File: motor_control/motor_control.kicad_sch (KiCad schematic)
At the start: 25 parts, among them J1 GPIO, J2 MotA, J3 MotB, J4 MOT_POW, J5 UART, J6 SPI, J7 I2C, J8 PEB_5V_IN, SW1 PU, SW2 PD, SW3 SW_SPDT_312, U1 HC-SR04

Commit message: update schematic text labels
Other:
- note added: "From PEB"
- note added: "To RPi"
- moved on the sheet: JP1
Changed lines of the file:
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@@
 		)
 	)
+	(text "From PEB"
+		(exclude_from_sim no)
+		(at 104.902 17.272 0)
+		(effects
+			(font
+				(size 1.27 1.27)
+			)
+		)
+	)
 	(text "From power expansion board"
 		(exclude_from_sim no)
@@
 		)
 	)
+	(text "To RPi"
+		(exclude_from_sim no)
+		(at 126.746 20.32 0)
+		(effects
+			(font
+				(size 1.27 1.27)
+			)
+		)
+	)
 	(text "To Motors"
 		(exclude_from_sim no)
@@
 	(wire
 		(pts
-			(xy 102.87 21.59) (xy 102.87 27.94)
+			(xy 95.25 21.59) (xy 95.25 27.94)
 		)
 		(stroke
@@
 	(wire
 		(pts
-			(xy 127 27.94) (xy 127 24.13)
+			(xy 119.38 27.94) (xy 119.38 24.13)
 		)
 		(stroke
@@
 	(wire
 		(pts
-			(xy 102.87 27.94) (xy 109.22 27.94)
+			(xy 95.25 27.94) (xy 101.6 27.94)
 		)
 		(stroke
@@
 	(wire
 		(pts
-			(xy 119.38 27.94) (xy 127 27.94)
+			(xy 111.76 27.94) (xy 119.38 27.94)
 		)
 		(stroke
@@
 	(symbol
 		(lib_id "power:+5V")
-		(at 102.87 21.59 0)
+		(at 95.25 21.59 0)
 		(unit 1)
 		(exclude_from_sim no)
@@
 		(dnp no)
 		(property "Reference" "#PWR031"
-			(at 102.87 25.4 0)
+			(at 95.25 25.4 0)
 			(effects
 				(font
@@
 		)
 		(property "Value" "5V_IN"
-			(at 103.2383 17.2656 0)
+			(at 95.6183 17.2656 0)
 			(effects
 				(font
@@
 		)
 		(property "Footprint" ""
-			(at 102.87 21.59 0)
+			(at 95.25 21.59 0)
 			(effects
 				(font
@@
 		)
 		(property "Datasheet" ""
-			(at 102.87 21.59 0)
+			(at 95.25 21.59 0)
 			(effects
 				(font
@@
 		)
 		(property "Description" "Power symbol creates a global label with name \"+5V\""
-			(at 102.87 21.59 0)
+			(at 95.25 21.59 0)
 			(effects
 				(font
@@
 	(symbol
 		(lib_id "power:+5V")
-		(at 127 24.13 0)
+		(at 119.38 24.13 0)
 		(unit 1)
 		(exclude_from_sim no)
@@
 		(dnp no)
 		(property "Reference" "#PWR030"
-			(at 127 27.94 0)
+			(at 119.38 27.94 0)
 			(effects
 				(font
@@
 		)
 		(property "Value" "+5V"
-			(at 127.3683 19.8056 0)
+			(at 119.7483 19.8056 0)
 			(effects
 				(font
@@
 		)
 		(property "Footprint" ""
-			(at 127 24.13 0)
+			(at 119.38 24.13 0)
 			(effects
 				(font
@@
 		)
 		(property "Datasheet" ""
-			(at 127 24.13 0)
+			(at 119.38 24.13 0)
 			(effects
 				(font
@@
 		)
 		(property "Description" "Power symbol creates a global label with name \"+5V\""
-			(at 127 24.13 0)
+			(at 119.38 24.13 0)
 			(effects
 				(font
@@
 	(symbol
 		(lib_id "Jumper:Jumper_2_Open")
-		(at 114.3 27.94 0)
+		(at 106.68 27.94 0)
 		(unit 1)
 		(exclude_from_sim no)
@@
 		(fields_autoplaced yes)
 		(property "Reference" "JP1"
-			(at 114.3 21.59 0)
+			(at 106.68 21.59 0)
 			(effects
 				(font
@@
 		)
 		(property "Value" "5V_PEB_RPi"
-			(at 114.3 24.13 0)
+			(at 106.68 24.13 0)
 			(effects
 				(font
@@
 		)
 		(property "Footprint" "Connector_PinHeader_2.54mm:PinHeader_1x02_P2.54mm_Vertical"
-			(at 114.3 27.94 0)
+			(at 106.68 27.94 0)
 			(effects
 				(font
@@
 		)
 		(property "Datasheet" "~"
-			(at 114.3 27.94 0)
+			(at 106.68 27.94 0)
 			(effects
 				(font
@@
 		)
 		(property "Description" "Jumper, 2-pole, open"
-			(at 114.3 27.94 0)
+			(at 106.68 27.94 0)
 			(effects
 				(font

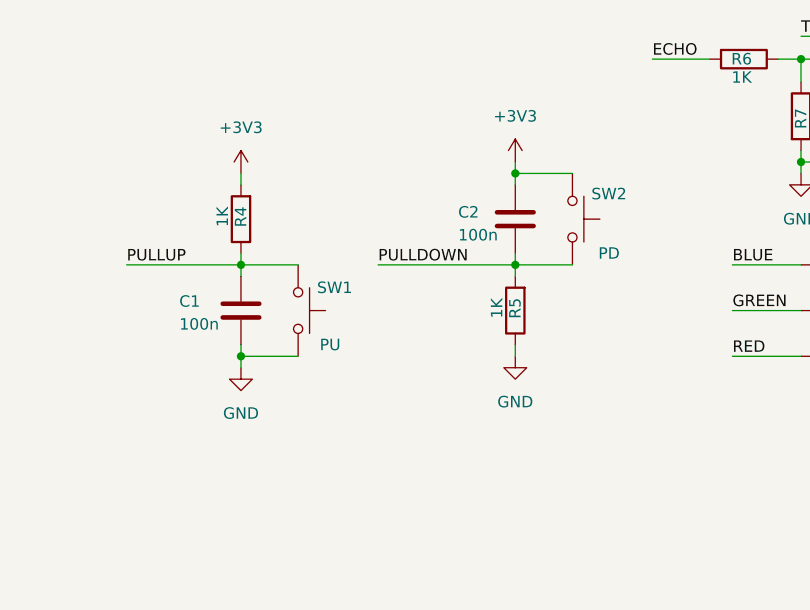
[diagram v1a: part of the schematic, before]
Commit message: update pull-down debouncer
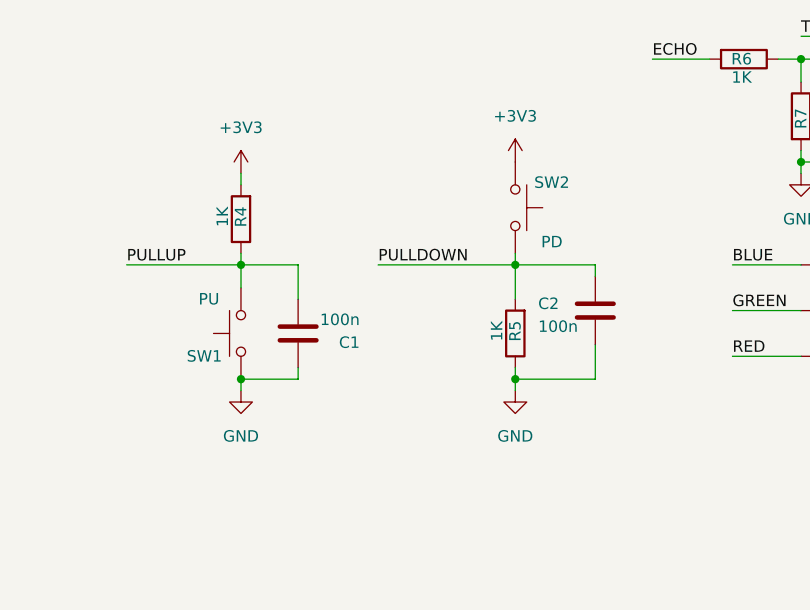
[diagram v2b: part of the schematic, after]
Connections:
- net +3V3: no longer C2.2
- net GND: now also C1.2, C2.1, SW1.1; no longer C1.1, SW1.2
- net PULLDOWN: now also C2.2; no longer C2.1
- net PULLUP: now also C1.1, SW1.2; no longer C1.2, SW1.1
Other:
- moved on the sheet: C1, C2, R5, SW1, SW2

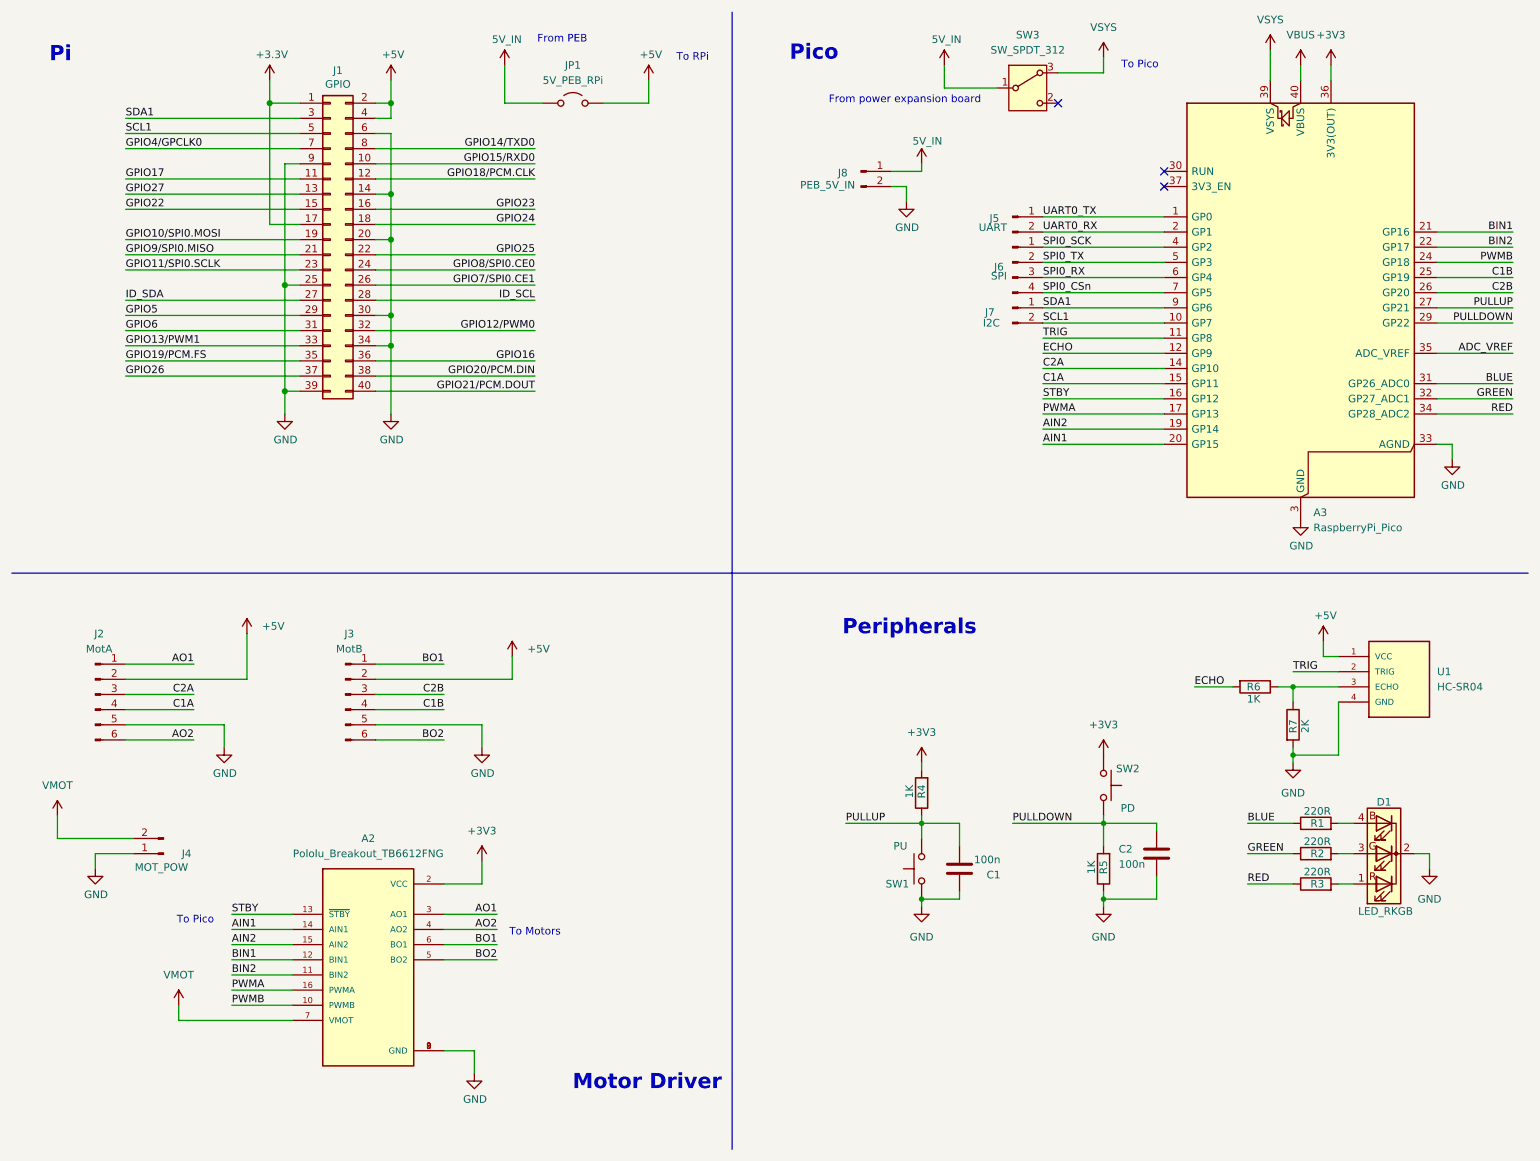
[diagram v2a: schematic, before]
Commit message: update REG_5V as source for all 5V components
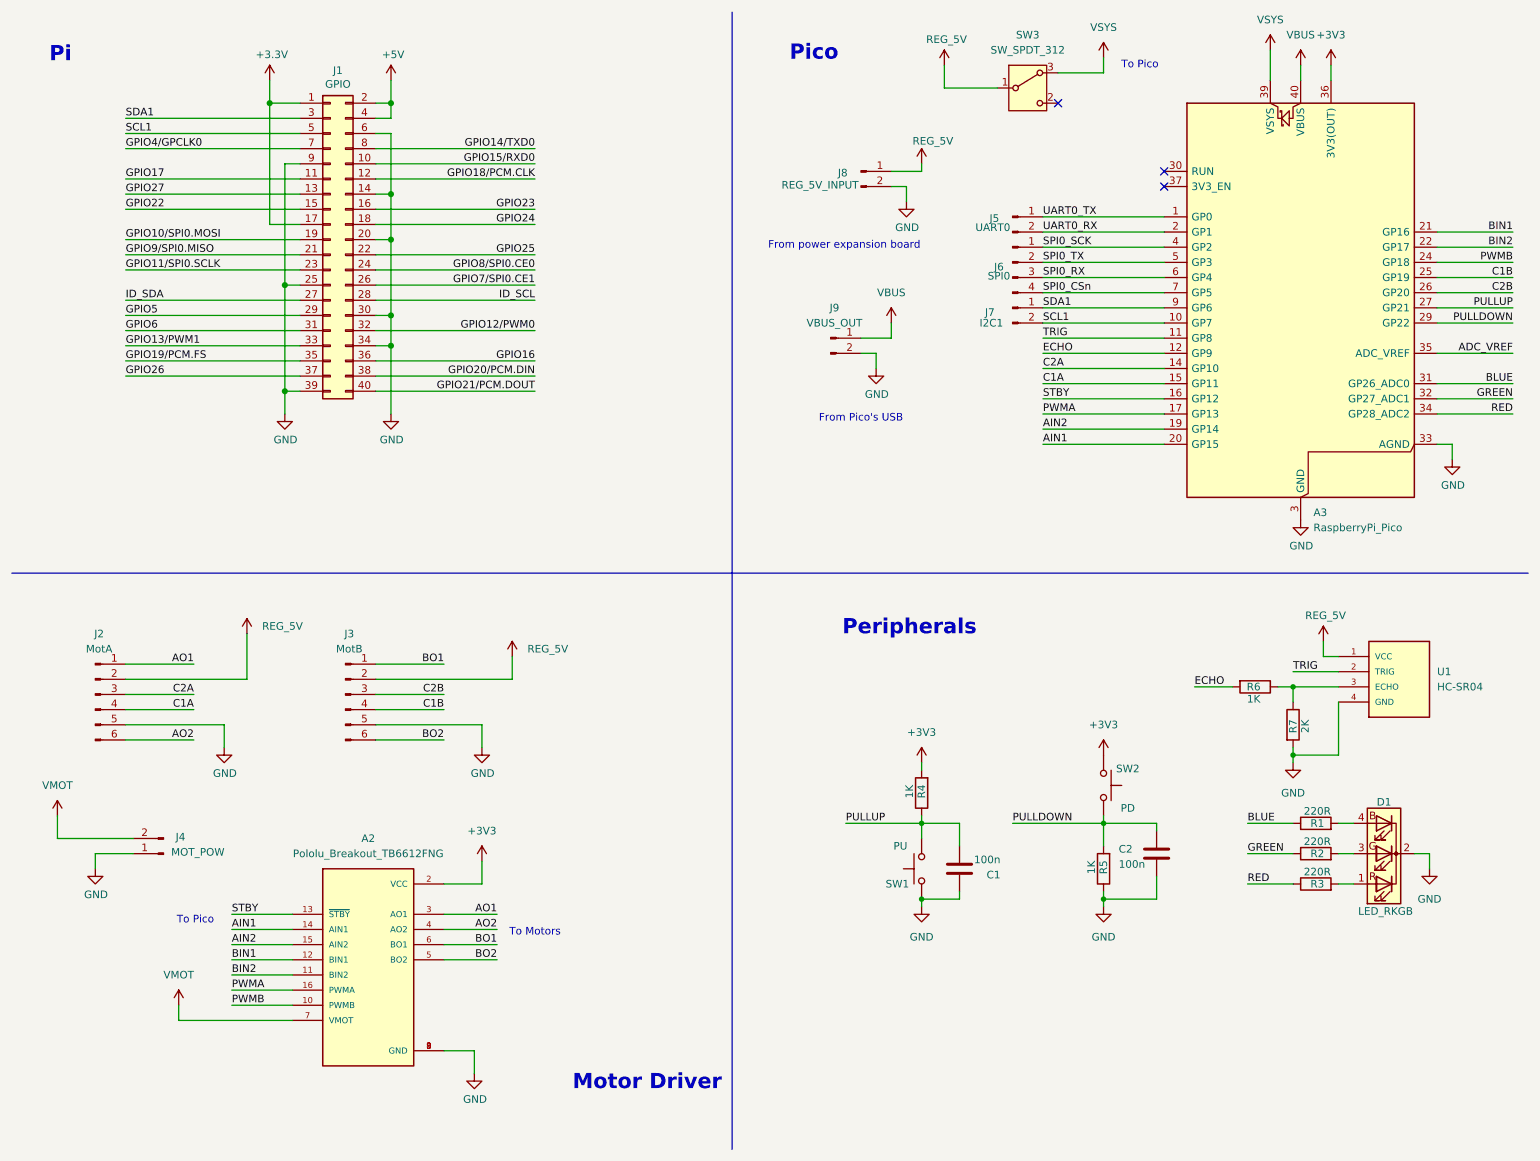
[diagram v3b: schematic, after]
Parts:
- removed JP1: 5V_PEB_RPi, Connector_PinHeader_2.54mm:PinHeader_1x02_P2.54mm_Vertical, symbol Jumper:Jumper_2_Open
- added J9: VBUS_OUT, symbol Connector:Conn_01x02_Pin
- J5: value UART -> UART0
- J6: value SPI -> SPI0
- J7: value I2C -> I2C1
- J8: value PEB_5V_IN -> REG_5V_INPUT
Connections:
- net +5V: no longer J2.2 (Pin_2), J3.2 (Pin_2), U1.1 (VCC)
- net GND: now also J9.2 (Pin_2)
- net VBUS: now also J9.1 (Pin_1)
- net 5V_IN renamed REG_5V
- net REG_5V: now also J2.2 (Pin_2), J3.2 (Pin_2), U1.1 (VCC)
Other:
- note added: "From Pico's USB"
- note removed: "From PEB"
- note removed: "To RPi"

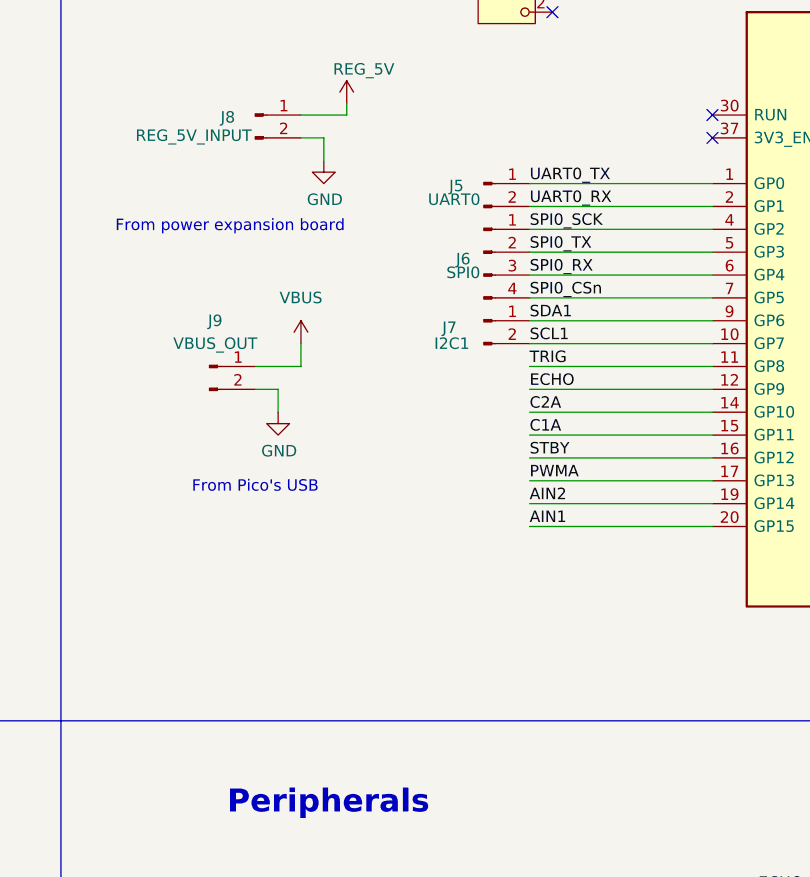
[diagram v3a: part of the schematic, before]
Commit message: update unused GP pins net labels
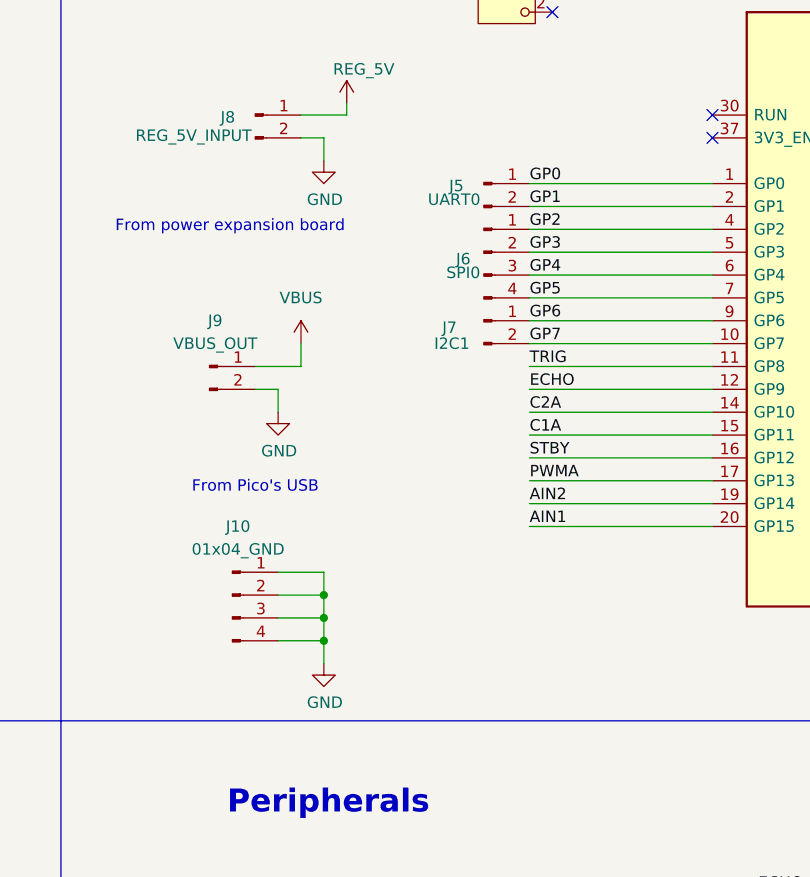
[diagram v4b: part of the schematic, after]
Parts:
- added J10: 01x04_GND, symbol Connector:Conn_01x04_Pin
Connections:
- net GND: now also J10.1 (Pin_1), J10.2 (Pin_2), J10.3 (Pin_3), J10.4 (Pin_4)
- net SCL1: no longer A3.10 (GP7), J7.2 (Pin_2)
- net SDA1: no longer A3.9 (GP6), J7.1 (Pin_1)
- net SPI0_CSn renamed GP5
- net SPI0_RX renamed GP4
- net SPI0_SCK renamed GP2
- net SPI0_TX renamed GP3
- net UART0_RX renamed GP1
- net UART0_TX renamed GP0
- new net GP6: A3.9 (GP6), J7.1 (Pin_1)
- new net GP7: A3.10 (GP7), J7.2 (Pin_2)
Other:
- company: UCA -> UCA Engineering Physics
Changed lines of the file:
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@@
 		(title "R1B Motor Controller")
 		(date "2025-07-20")
-		(rev "0")
-		(company "UCA")
+		(rev "1")
+		(company "UCA Engineering Physics")
 	)
 	(text "Pico"
@@
 	)
 	(junction
+		(at 162.56 95.25)
+		(diameter 0)
+		(color 0 0 0 0)
+	)
+	(junction
 		(at 165.1 148.59)
 		(diameter 0)
@@
 	)
 	(junction
+		(at 162.56 92.71)
+		(diameter 0)
+		(color 0 0 0 0)
+	)
+	(junction
 		(at 58.42 58.42)
 		(diameter 1.016)
@@
 	)
 	(junction
+		(at 162.56 97.79)
+		(diameter 0)
+		(color 0 0 0 0)
+	)
+	(junction
 		(at 165.1 161.29)
 		(diameter 0)
@@
 	(wire
 		(pts
+			(xy 162.56 92.71) (xy 162.56 95.25)
+		)
+		(stroke
+			(width 0)
+			(type default)
+		)
+	)
+	(wire
+		(pts
 			(xy 254 85.09) (xy 254 87.63)
 		)
@@
 	(wire
 		(pts
+			(xy 157.48 90.17) (xy 162.56 90.17)
+		)
+		(stroke
+			(width 0)
+			(type default)
+		)
+	)
+	(wire
+		(pts
 			(xy 195.58 22.86) (xy 187.96 22.86)
 		)
@@
 	(wire
 		(pts
+			(xy 162.56 97.79) (xy 162.56 100.33)
+		)
+		(stroke
+			(width 0)
+			(type default)
+		)
+	)
+	(wire
+		(pts
 			(xy 76.2 50.8) (xy 76.2 63.5)
 		)
@@
 	(wire
 		(pts
+			(xy 157.48 97.79) (xy 162.56 97.79)
+		)
+		(stroke
+			(width 0)
+			(type default)
+		)
+	)
+	(wire
+		(pts
 			(xy 251.46 57.15) (xy 264.16 57.15)
 		)
@@
 	(wire
 		(pts
+			(xy 157.48 95.25) (xy 162.56 95.25)
+		)
+		(stroke
+			(width 0)
+			(type default)
+		)
+	)
+	(wire
+		(pts
 			(xy 60.96 30.48) (xy 31.75 30.48)
 		)
@@
 	(wire
 		(pts
+			(xy 157.48 92.71) (xy 162.56 92.71)
+		)
+		(stroke
+			(width 0)
+			(type default)
+		)
+	)
+	(wire
+		(pts
 			(xy 76.2 24.13) (xy 76.2 27.94)
 		)
@@
 	(wire
 		(pts
+			(xy 162.56 95.25) (xy 162.56 97.79)
+		)
+		(stroke
+			(width 0)
+			(type default)
+		)
+	)
+	(wire
+		(pts
 			(xy 48.26 132.08) (xy 48.26 135.89)
 		)
@@
 	(wire
 		(pts
+			(xy 162.56 90.17) (xy 162.56 92.71)
+		)
+		(stroke
+			(width 0)
+			(type default)
+		)
+	)
+	(wire
+		(pts
 			(xy 168.91 25.4) (xy 177.8 25.4)
 		)
@@
 		)
 	)
-	(label "SPI0_CSn"
+	(label "GP5"
 		(at 185.42 59.69 0)
 		(effects
@@
 		)
 	)
-	(label "UART0_TX"
+	(label "GP0"
 		(at 185.42 46.99 0)
 		(effects
@@
 		)
 	)
-	(label "UART0_RX"
+	(label "GP1"
 		(at 185.42 49.53 0)
 		(effects
@@
 		)
 	)
-	(label "SPI0_TX"
+	(label "GP3"
 		(at 185.42 54.61 0)
 		(effects
@@
 		)
 	)
-	(label "SPI0_SCK"
+	(label "GP2"
 		(at 185.42 52.07 0)
 		(effects
@@
 		)
 	)
-	(label "SCL1"
+	(label "GP7"
 		(at 185.42 64.77 0)
 		(effects
@@
 		)
 	)
-	(label "SPI0_RX"
+	(label "GP4"
 		(at 185.42 57.15 0)
 		(effects
@@
 		)
 	)
-	(label "SDA1"
+	(label "GP6"
 		(at 185.42 62.23 0)
 		(effects
@@
 					(unit 1)
 				)
+			)
+		)
+	)
+	(symbol
+		(lib_id "Connector:Conn_01x04_Pin")
+		(at 152.4 92.71 0)
+		(unit 1)
+		(exclude_from_sim no)
+		(in_bom yes)
+		(on_board yes)
+		(dnp no)
+		(fields_autoplaced yes)
+		(property "Reference" "J10"
+			(at 153.035 85.09 0)
+			(effects
+				(font
+					(size 1.27 1.27)
+				)
+			)
+		)
+		(property "Value" "01x04_GND"
+			(at 153.035 87.63 0)
+			(effects
+				(font
+					(size 1.27 1.27)
+				)
+			)
+		)
+		(property "Footprint" ""
+			(at 152.4 92.71 0)
+			(effects
+				(font
+					(size 1.27 1.27)
+				)
+				(hide yes)
+			)
+		)
+		(property "Datasheet" "~"
+			(at 152.4 92.71 0)
+			(effects
+				(font
+					(size 1.27 1.27)
+				)
+				(hide yes)
+			)
+		)
+		(property "Description" "Generic connector, single row, 01x04, script generated"
+			(at 152.4 92.71 0)
+			(effects
+				(font
+					(size 1.27 1.27)
+				)
+				(hide yes)
+			)
+		)
+		(pin "1"
+		)
+		(pin "4"
+		)
+		(pin "3"
+		)
+		(pin "2"
+		)
+		(instances
+			(project ""
+				(path "/e63e39d7-6ac0-4ffd-8aa3-1841a4541b55"
+					(reference "J10")
+					(unit 1)
+				)
+			)
+		)
+	)
+	(symbol
+		(lib_id "power:GND")
+		(at 162.56 100.33 0)
+		(unit 1)
+		(exclude_from_sim no)
+		(in_bom yes)
+		(on_board yes)
+		(dnp no)
+		(property "Reference" "#PWR032"
+			(at 162.56 106.68 0)
+			(effects
+				(font
+					(size 1.27 1.27)
+				)
+				(hide yes)
+			)
+		)
+		(property "Value" "GND"
+			(at 162.6743 104.6544 0)
+			(effects
+				(font
+					(size 1.27 1.27)
+				)
+			)
+		)
+		(property "Footprint" ""
+			(at 162.56 100.33 0)
+			(effects
+				(font
+					(size 1.27 1.27)
+				)
+			)
+		)
+		(property "Datasheet" ""
+			(at 162.56 100.33 0)
+			(effects
+				(font
+					(size 1.27 1.27)
+				)
+			)
+		)
+		(property "Description" "Power symbol creates a global label with name \"GND\" , ground"
+			(at 162.56 100.33 0)
+			(effects
+				(font
+					(size 1.27 1.27)
+				)
+				(hide yes)
+			)
+		)
+		(pin "1"
+		)
+		(instances
+			(project "motor_control"
+				(path "/e63e39d7-6ac0-4ffd-8aa3-1841a4541b55"
+					(reference "#PWR032")
+					(unit 1)
+				)
